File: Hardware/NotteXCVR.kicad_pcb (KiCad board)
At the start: 2 copper layers, 22 x 30 mm, 2 parts, among them J1 Bus_M.2_Socket_E, U1 XC7A50T-CPG236

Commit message: CSG325?
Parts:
- removed U1: XC7A50T-CPG236, Package_BGA:Xilinx_CPG236
- added R1: 100, Resistor_SMD:R_0402_1005Metric, F.Cu at (132.3, 104.9)
- added U2: XC7A35T-CSG325, Package_BGA:Xilinx_CSG325, F.Cu at (137.9, 125.0)

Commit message: PCIe
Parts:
- J1: value Bus_M.2_Socket_E -> Bus_PCI_Express_x1; footprint Connector_PCBEdge:M.2_2230-xx-E -> Connector_PCBEdge:BUS_PCIexpress_x1
- moved U2 65.9 mm to (89.9, 79.9), turned to 90 degrees
- moved R1 55.9 mm to (77.9, 92.0)
- moved J1 35.4 mm to (77.3, 102.7)
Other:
- board size 22 x 30 mm -> 20.3 x 8.4 mm

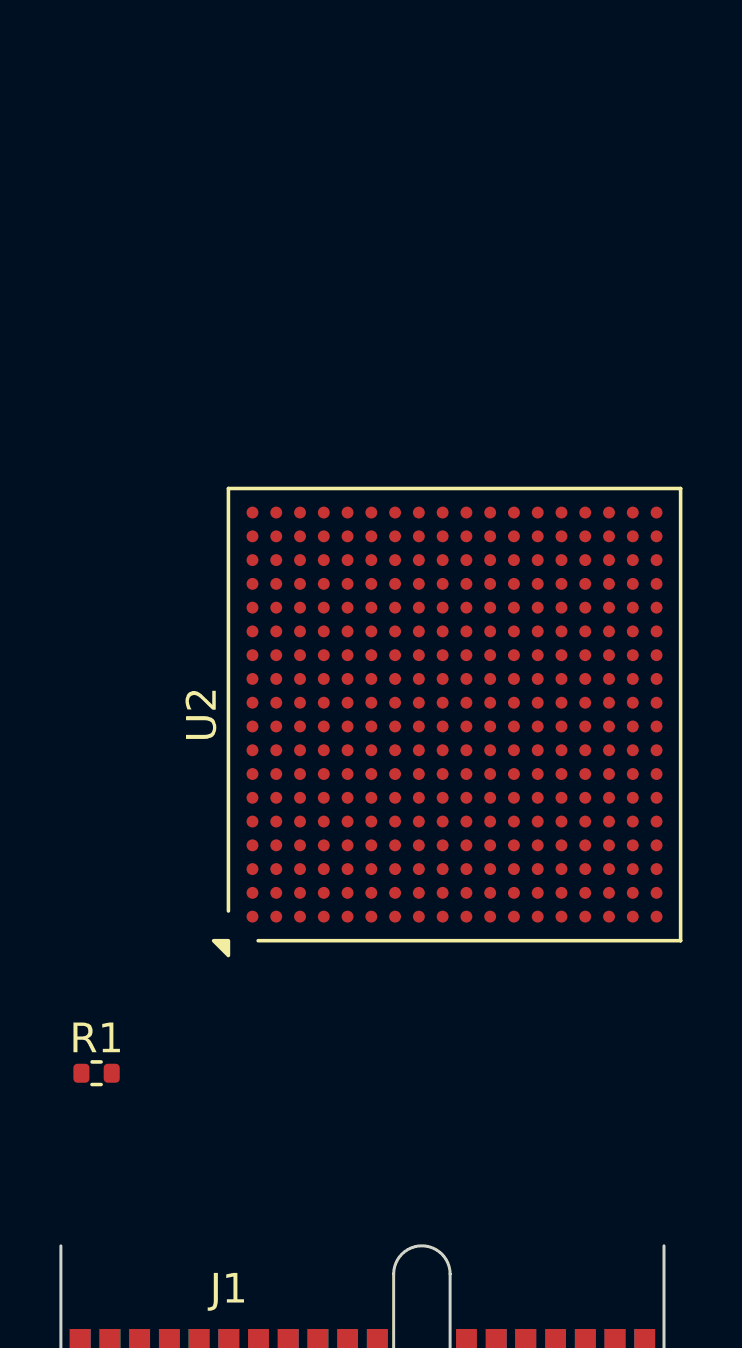
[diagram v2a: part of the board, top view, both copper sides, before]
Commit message: Added LGA connector, to be used for configuration interface
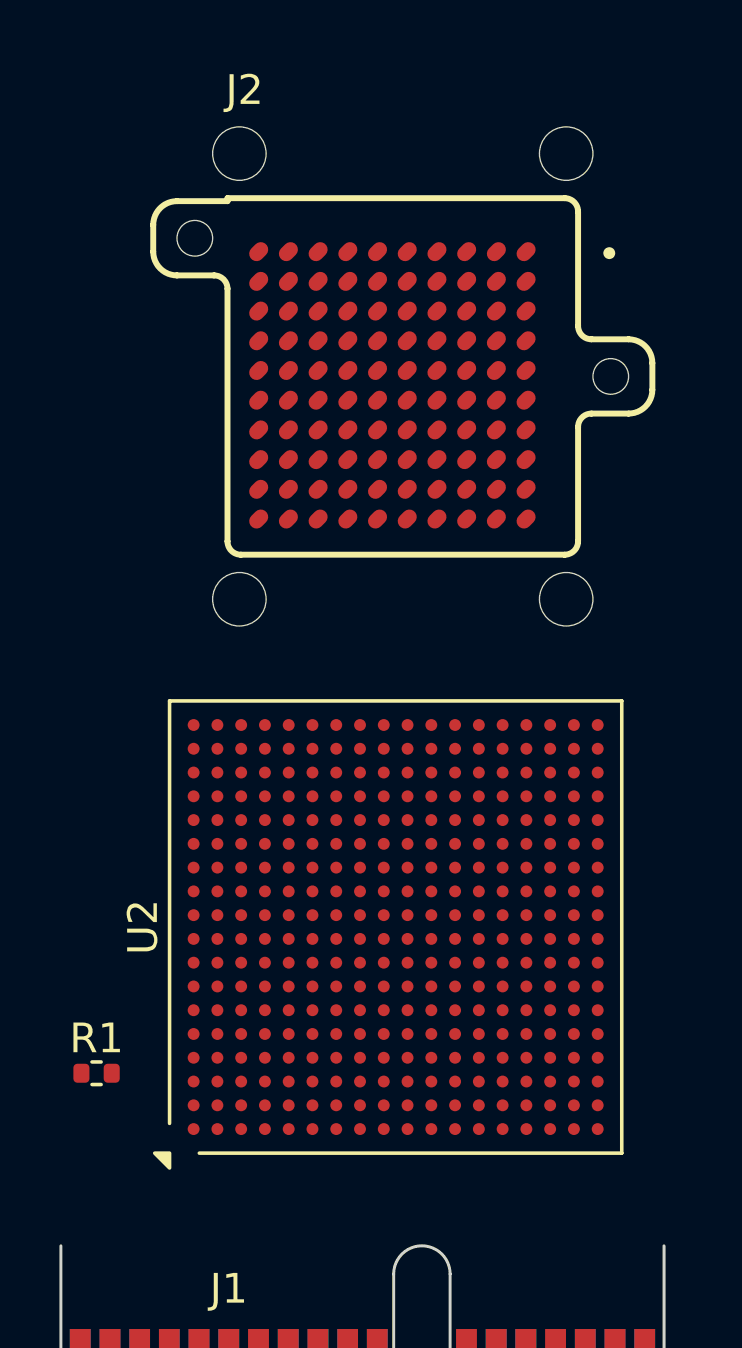
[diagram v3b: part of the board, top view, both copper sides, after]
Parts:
- added J2: GMI-10-2-1.27-G-10, GMI-10-2-1.27-G-10:SAMTEC_GMI-10-2-1.27-G-10, F.Cu at (88.2, 68.5)
- moved U2 7.42 mm to (88.0, 87.1)
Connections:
- R1 pad 1: unconnected-(R1-Pad1) -> Net-(R1-Pad1)
- R1 pad 2: unconnected-(R1-Pad2) -> Net-(U2D-MGTRREF_216)
- U2 pad A2: unconnected-(U2D-MGTAVTT-PadA2) -> Net-(R1-Pad1)
- U2 pad A6: unconnected-(U2D-MGTRREF_216-PadA6) -> Net-(U2D-MGTRREF_216)
- U2 pad C1: unconnected-(U2D-MGTAVTT-PadC1) -> Net-(R1-Pad1)
- U2 pad E1: unconnected-(U2D-MGTAVTT-PadE1) -> Net-(R1-Pad1)
- U2 pad F3: unconnected-(U2D-MGTAVTT-PadF3) -> Net-(R1-Pad1)
- U2 pad G2: unconnected-(U2D-MGTAVTT-PadG2) -> Net-(R1-Pad1)

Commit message: Trying to assign MGT lanes but I don't know how to do inter sheet connectivity yet
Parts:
- added C1: 0.01uF, Capacitor_SMD:C_0402_1005Metric, F.Cu at (91.3, 96.3)
- added C2: 0.01uF, Capacitor_SMD:C_0402_1005Metric, F.Cu at (92.4, 96.2)
- added C3: 0.22uF, Capacitor_SMD:C_0402_1005Metric, F.Cu at (94.3, 96.2)
- added C4: 0.22uF, Capacitor_SMD:C_0402_1005Metric, F.Cu at (95.5, 96.2)
- moved R1 2.11 mm to (77.9, 89.9)
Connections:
- net Net-(J1-+12V-PadA2) renamed +12V
- net Net-(J1-+3.3V-PadA10) renamed +3.3V
- net Net-(R1-Pad1) renamed MGTAVTT
- J1 pad A13: unconnected-(J1-REFCLK+-PadA13) -> Net-(J1-REFCLK+)
- J1 pad A14: unconnected-(J1-REFCLK--PadA14) -> Net-(J1-REFCLK-)
- J1 pad A16: unconnected-(J1-PERp0-PadA16) -> Net-(J1-PERp0)
- J1 pad A17: unconnected-(J1-PERn0-PadA17) -> Net-(J1-PERn0)
- J1 pad B14: unconnected-(J1-PETp0-PadB14) -> /PCIE_Edge/PCIE_TX_P
- J1 pad B15: unconnected-(J1-PETn0-PadB15) -> /PCIE_Edge/PCIE_TX_N
- U2 pad B4: unconnected-(U2D-MGTAVCC-PadB4) -> MGTAVCC
- U2 pad C3: unconnected-(U2C-MGTPRXN2_216-PadC3) -> /FPGA_MGT/MGT_LOOPBACK_N
- U2 pad C4: unconnected-(U2C-MGTPRXP2_216-PadC4) -> /FPGA_MGT/MGT_LOOPBACK_P
- U2 pad C5: unconnected-(U2D-MGTAVCC-PadC5) -> MGTAVCC
- U2 pad D1: unconnected-(U2C-MGTPTXN2_216-PadD1) -> /FPGA_MGT/MGT_LOOPBACK_N
- U2 pad D2: unconnected-(U2C-MGTPTXP2_216-PadD2) -> /FPGA_MGT/MGT_LOOPBACK_P
- U2 pad E5: unconnected-(U2D-MGTAVCC-PadE5) -> MGTAVCC
- U2 pad F5: unconnected-(U2D-MGTAVCC-PadF5) -> MGTAVCC
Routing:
- net Net-(U2D-MGTRREF_216): track 0.00 -> 2.76 mm

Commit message: Found the global labels
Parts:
- C1, C2, C3, C4: moved to B.Cu
- moved R1 9.49 mm to (87.1, 87.4)
- moved U2 9.49 mm to (97.1, 84.6)
- moved J2 3.68 mm to (86.7, 65.2)
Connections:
- C1 pad 1: /PCIE_Edge/PCIE_REFCLK_P -> PCIE_REFCLK_P
- C2 pad 1: /PCIE_Edge/PCIE_REFCLK_N -> PCIE_REFCLK_N
- C3 pad 2: /PCIE_Edge/PCIE_RX_P -> PCIE_RX_P
- C4 pad 2: /PCIE_Edge/PCIE_RX_N -> PCIE_RX_N
- J1 pad A12: Net-(J1-GND-PadA12) -> GND
- J1 pad A15: Net-(J1-GND-PadA12) -> GND
- J1 pad A18: Net-(J1-GND-PadA12) -> GND
- J1 pad A4: Net-(J1-GND-PadA12) -> GND
- J1 pad B13: Net-(J1-GND-PadA12) -> GND
- J1 pad B14: /PCIE_Edge/PCIE_TX_P -> PCIE_TX_P
- J1 pad B15: /PCIE_Edge/PCIE_TX_N -> PCIE_TX_N
- J1 pad B16: Net-(J1-GND-PadA12) -> GND
- J1 pad B18: Net-(J1-GND-PadA12) -> GND
- J1 pad B4: Net-(J1-GND-PadA12) -> GND
- J1 pad B7: Net-(J1-GND-PadA12) -> GND
- J2 pad A01: unconnected-(J2-PadA01) -> GND
- J2 pad A04: unconnected-(J2-PadA04) -> GND
- J2 pad A07: unconnected-(J2-PadA07) -> GND
- J2 pad A10: unconnected-(J2-PadA10) -> GND
- J2 pad D01: unconnected-(J2-PadD01) -> GND
- J2 pad D04: unconnected-(J2-PadD04) -> GND
- J2 pad D07: unconnected-(J2-PadD07) -> GND
- J2 pad D10: unconnected-(J2-PadD10) -> GND
- J2 pad G01: unconnected-(J2-PadG01) -> GND
- J2 pad G04: unconnected-(J2-PadG04) -> GND
- J2 pad G07: unconnected-(J2-PadG07) -> GND
- J2 pad G10: unconnected-(J2-PadG10) -> GND
- J2 pad J01: unconnected-(J2-PadJ01) -> GND
- J2 pad J04: unconnected-(J2-PadJ04) -> GND
- J2 pad J07: unconnected-(J2-PadJ07) -> GND
- J2 pad J10: unconnected-(J2-PadJ10) -> GND
- U2 pad A3: unconnected-(U2C-MGTPRXN1_216-PadA3) -> /FPGA_MGT/MGT_SMA_RX_N
- U2 pad A4: unconnected-(U2C-MGTPRXP1_216-PadA4) -> /FPGA_MGT/MGT_SMA_RX_P
- U2 pad B1: unconnected-(U2C-MGTPTXN3_216-PadB1) -> PCIE_TX_N
- U2 pad B2: unconnected-(U2C-MGTPTXP3_216-PadB2) -> PCIE_TX_P
- U2 pad B5: unconnected-(U2C-MGTREFCLK1N_216-PadB5) -> PCIE_REFCLK_N
- U2 pad B6: unconnected-(U2C-MGTREFCLK1P_216-PadB6) -> PCIE_REFCLK_P
- U2 pad D5: unconnected-(U2C-MGTREFCLK0N_216-PadD5) -> /FPGA_MGT/SMA_CLK_N
- U2 pad D6: unconnected-(U2C-MGTREFCLK0P_216-PadD6) -> /FPGA_MGT/SMA_CLK_P
- U2 pad F1: unconnected-(U2C-MGTPTXN1_216-PadF1) -> /FPGA_MGT/MGT_SMA_TX_N
- U2 pad F2: unconnected-(U2C-MGTPTXP1_216-PadF2) -> /FPGA_MGT/MGT_SMA_TX_P
- U2 pad G3: unconnected-(U2C-MGTPRXN3_216-PadG3) -> PCIE_RX_N
- U2 pad G4: unconnected-(U2C-MGTPRXP3_216-PadG4) -> PCIE_RX_P
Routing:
- net /FPGA_MGT/MGT_LOOPBACK_P: track 0.00 -> 2.61 mm
- net /FPGA_MGT/MGT_LOOPBACK_N: track 0.00 -> 2.58 mm
- net PCIE_RX_P: track 0.00 -> 0.43 mm, vias 0 -> 1
- net PCIE_RX_N: track 0.00 -> 0.41 mm, vias 0 -> 1

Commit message: Is this orientation better
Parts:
- added J3: Conn_Coaxial, Connector_Coaxial:U.FL_Hirose_U.FL-R-SMT-1_Vertical, F.Cu at (85.1, 74.1)
- added J4: Conn_Coaxial, Connector_Coaxial:U.FL_Hirose_U.FL-R-SMT-1_Vertical, F.Cu at (87.1, 69.7)
- added J5: Conn_Coaxial, Connector_Coaxial:U.FL_Hirose_U.FL-R-SMT-1_Vertical, F.Cu at (91.2, 74.1)
- added J6: Conn_Coaxial, Connector_Coaxial:U.FL_Hirose_U.FL-R-SMT-1_Vertical, F.Cu at (93.2, 69.8)
- added J7: Conn_Coaxial, Connector_Coaxial:U.FL_Hirose_U.FL-R-SMT-1_Vertical, F.Cu at (79.2, 74.1)
- added J8: Conn_Coaxial, Connector_Coaxial:U.FL_Hirose_U.FL-R-SMT-1_Vertical, F.Cu at (81.3, 69.6)
- moved U2 10.0 mm to (87.1, 84.9), turned to 180 degrees
- moved R1 7.30 mm to (90.5, 93.9), turned to 180 degrees
- moved J2 6.25 mm to (86.8, 58.9)
- moved C2 0.11 mm to (92.4, 96.3)
- moved C1 0.11 mm to (91.4, 96.4)
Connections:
- C3 pad 2: PCIE_RX_P -> PCIE_TX_P
- C4 pad 2: PCIE_RX_N -> PCIE_TX_N
- J1 pad B14: PCIE_TX_P -> PCIE_RX_P
- J1 pad B15: PCIE_TX_N -> PCIE_RX_N
- U2 pad A1: unconnected-(U2F-GND-PadA1) -> GND
- U2 pad A11: unconnected-(U2F-GND-PadA11) -> GND
- U2 pad A16: unconnected-(U2A-VCCO_15-PadA16) -> Net-(U2A-VCCO_15-PadA16)
- U2 pad A18: unconnected-(U2F-GND-PadA18) -> GND
- U2 pad A3: /FPGA_MGT/MGT_SMA_RX_N -> /FPGA_MGT/MGT_UFL_RX_N
- U2 pad A4: /FPGA_MGT/MGT_SMA_RX_P -> /FPGA_MGT/MGT_UFL_RX_P
- U2 pad A5: unconnected-(U2F-GND-PadA5) -> GND
- U2 pad A7: unconnected-(U2F-GND-PadA7) -> GND
- U2 pad A8: unconnected-(U2F-GND-PadA8) -> GND
- U2 pad B13: unconnected-(U2A-VCCO_15-PadB13) -> Net-(U2A-VCCO_15-PadA16)
- U2 pad B18: unconnected-(U2F-GND-PadB18) -> GND
- U2 pad B3: unconnected-(U2F-GND-PadB3) -> GND
- U2 pad B7: unconnected-(U2F-GND-PadB7) -> GND
- U2 pad B8: unconnected-(U2F-GND-PadB8) -> GND
- U2 pad C10: unconnected-(U2A-VCCO_15-PadC10) -> Net-(U2A-VCCO_15-PadA16)
- U2 pad C15: unconnected-(U2F-GND-PadC15) -> GND
- U2 pad C2: unconnected-(U2F-GND-PadC2) -> GND
- U2 pad C6: unconnected-(U2F-GND-PadC6) -> GND
- U2 pad C7: unconnected-(U2F-GND-PadC7) -> GND
- U2 pad D12: unconnected-(U2F-GND-PadD12) -> GND
- U2 pad D17: unconnected-(U2A-VCCO_15-PadD17) -> Net-(U2A-VCCO_15-PadA16)
- U2 pad D3: unconnected-(U2F-GND-PadD3) -> GND
- U2 pad D4: unconnected-(U2F-GND-PadD4) -> GND
- U2 pad D5: /FPGA_MGT/SMA_CLK_N -> /FPGA_MGT/UFL_CLK_N
- U2 pad D6: /FPGA_MGT/SMA_CLK_P -> /FPGA_MGT/UFL_CLK_P
- U2 pad D7: unconnected-(U2F-GND-PadD7) -> GND
- U2 pad E11: unconnected-(U2F-VCCBATT_0-PadE11) -> +1V8
- U2 pad E14: unconnected-(U2A-VCCO_15-PadE14) -> Net-(U2A-VCCO_15-PadA16)
- U2 pad E2: unconnected-(U2F-GND-PadE2) -> GND
- U2 pad E6: unconnected-(U2F-GND-PadE6) -> GND
- U2 pad E7: unconnected-(U2F-GND-PadE7) -> GND
- U2 pad E9: unconnected-(U2F-GND-PadE9) -> GND
- U2 pad F1: /FPGA_MGT/MGT_SMA_TX_N -> /FPGA_MGT/MGT_UFL_TX_N
- U2 pad F10: unconnected-(U2F-GND-PadF10) -> GND
- U2 pad F11: unconnected-(U2F-VCCBRAM-PadF11) -> +1V0
- U2 pad F16: unconnected-(U2F-GND-PadF16) -> GND
- U2 pad F2: /FPGA_MGT/MGT_SMA_TX_P -> /FPGA_MGT/MGT_UFL_TX_P
- U2 pad F4: unconnected-(U2F-GND-PadF4) -> GND
- U2 pad F6: unconnected-(U2F-GND-PadF6) -> GND
- U2 pad F7: unconnected-(U2F-VCCINT-PadF7) -> +1V0
- U2 pad F9: unconnected-(U2F-VCCINT-PadF9) -> +1V0
- U2 pad G1: unconnected-(U2F-GND-PadG1) -> GND
- U2 pad G10: unconnected-(U2F-VCCBRAM-PadG10) -> +1V0
- U2 pad G11: unconnected-(U2F-GND-PadG11) -> GND
- U2 pad G12: unconnected-(U2F-VCCAUX-PadG12) -> +1V8
- U2 pad G13: unconnected-(U2F-GND-PadG13) -> GND
- U2 pad G18: unconnected-(U2A-VCCO_15-PadG18) -> Net-(U2A-VCCO_15-PadA16)
- U2 pad G5: unconnected-(U2F-GND-PadG5) -> GND
- U2 pad G6: unconnected-(U2F-GND-PadG6) -> GND
- U2 pad G7: unconnected-(U2F-GND-PadG7) -> GND
- U2 pad G8: unconnected-(U2F-VCCINT-PadG8) -> +1V0
- U2 pad G9: unconnected-(U2F-GND-PadG9) -> GND
- U2 pad H10: unconnected-(U2F-GND-PadH10) -> GND
- U2 pad H11: unconnected-(U2F-VCCBRAM-PadH11) -> +1V0
- U2 pad H12: unconnected-(U2F-GND-PadH12) -> GND
- U2 pad H13: unconnected-(U2F-VCCAUX-PadH13) -> +1V8
- U2 pad H15: unconnected-(U2A-VCCO_15-PadH15) -> Net-(U2A-VCCO_15-PadA16)
- U2 pad H3: unconnected-(U2F-GND-PadH3) -> GND
- U2 pad H4: unconnected-(U2F-GND-PadH4) -> GND
- U2 pad H5: unconnected-(U2F-GND-PadH5) -> GND
- U2 pad H6: unconnected-(U2F-GND-PadH6) -> GND
- U2 pad H7: unconnected-(U2F-VCCINT-PadH7) -> +1V0
- U2 pad H8: unconnected-(U2F-GND-PadH8) -> GND
- U2 pad H9: unconnected-(U2F-VCCINT-PadH9) -> +1V0
- U2 pad J1: unconnected-(U2F-GND-PadJ1) -> GND
- U2 pad J10: unconnected-(U2F-VCCADC_0-PadJ10) -> +1V8
- U2 pad J11: unconnected-(U2F-GND-PadJ11) -> GND
- U2 pad J12: unconnected-(U2F-VCCINT-PadJ12) -> +1V0
- U2 pad J13: unconnected-(U2F-GND-PadJ13) -> GND
- U2 pad J17: unconnected-(U2F-GND-PadJ17) -> GND
- U2 pad J2: unconnected-(U2F-GND-PadJ2) -> GND
- U2 pad J3: unconnected-(U2F-GND-PadJ3) -> GND
- U2 pad J7: unconnected-(U2F-GND-PadJ7) -> GND
- U2 pad J8: unconnected-(U2F-VCCINT-PadJ8) -> +1V0
- U2 pad J9: unconnected-(U2F-GNDADC_0-PadJ9) -> GND
- U2 pad K11: unconnected-(U2F-VCCINT-PadK11) -> +1V0
- U2 pad K12: unconnected-(U2F-GND-PadK12) -> GND
- U2 pad K13: unconnected-(U2F-VCCAUX-PadK13) -> +1V8
- U2 pad K14: unconnected-(U2F-GND-PadK14) -> GND
- U2 pad K4: unconnected-(U2F-GND-PadK4) -> GND
- U2 pad K7: unconnected-(U2F-VCCINT-PadK7) -> +1V0
- U2 pad K8: unconnected-(U2F-GND-PadK8) -> GND
- U2 pad L1: unconnected-(U2F-GND-PadL1) -> GND
- U2 pad L11: unconnected-(U2F-GND-PadL11) -> GND
- U2 pad L12: unconnected-(U2F-VCCINT-PadL12) -> +1V0
- U2 pad L13: unconnected-(U2F-GND-PadL13) -> GND
- U2 pad L16: unconnected-(U2A-VCCO_14-PadL16) -> Net-(U2A-VCCO_14-PadL16)
- U2 pad L6: unconnected-(U2B-VCCO_34-PadL6) -> Net-(U2B-VCCO_34-PadL6)
- U2 pad L7: unconnected-(U2F-GND-PadL7) -> GND
- U2 pad L8: unconnected-(U2F-VCCINT-PadL8) -> +1V0
- U2 pad M11: unconnected-(U2F-VCCINT-PadM11) -> +1V0
- U2 pad M12: unconnected-(U2F-GND-PadM12) -> GND
- U2 pad M13: unconnected-(U2F-VCCAUX-PadM13) -> +1V8
- U2 pad M18: unconnected-(U2F-GND-PadM18) -> GND
- U2 pad M3: unconnected-(U2B-VCCO_34-PadM3) -> Net-(U2B-VCCO_34-PadL6)
- U2 pad M7: unconnected-(U2F-VCCINT-PadM7) -> +1V0
- U2 pad M8: unconnected-(U2F-GND-PadM8) -> GND
- U2 pad N10: unconnected-(U2F-VCCINT-PadN10) -> +1V0
- U2 pad N11: unconnected-(U2F-GND-PadN11) -> GND
- U2 pad N12: unconnected-(U2F-VCCINT-PadN12) -> +1V0
- U2 pad N13: unconnected-(U2F-GND-PadN13) -> GND
- U2 pad N15: unconnected-(U2F-GND-PadN15) -> GND
- U2 pad N5: unconnected-(U2F-GND-PadN5) -> GND
- U2 pad N7: unconnected-(U2F-GND-PadN7) -> GND
- U2 pad N8: unconnected-(U2F-VCCINT-PadN8) -> +1V0
- U2 pad N9: unconnected-(U2F-GND-PadN9) -> GND
- U2 pad P11: unconnected-(U2F-VCCINT-PadP11) -> +1V0
- U2 pad P12: unconnected-(U2F-GND-PadP12) -> GND
- U2 pad P13: unconnected-(U2F-VCCAUX-PadP13) -> +1V8
- U2 pad P17: unconnected-(U2A-VCCO_14-PadP17) -> Net-(U2A-VCCO_14-PadL16)
- U2 pad P2: unconnected-(U2F-GND-PadP2) -> GND
- U2 pad P7: unconnected-(U2B-VCCO_34-PadP7) -> Net-(U2B-VCCO_34-PadL6)
- U2 pad P8: unconnected-(U2F-GND-PadP8) -> GND
- U2 pad P9: unconnected-(U2F-VCCINT-PadP9) -> +1V0
- U2 pad R14: unconnected-(U2A-VCCO_14-PadR14) -> Net-(U2A-VCCO_14-PadL16)
- U2 pad R4: unconnected-(U2B-VCCO_34-PadR4) -> Net-(U2B-VCCO_34-PadL6)
- U2 pad R9: unconnected-(U2F-GND-PadR9) -> GND
- U2 pad T1: unconnected-(U2B-VCCO_34-PadT1) -> Net-(U2B-VCCO_34-PadL6)
- U2 pad T11: unconnected-(U2A-VCCO_14-PadT11) -> Net-(U2A-VCCO_14-PadL16)
- U2 pad T16: unconnected-(U2F-GND-PadT16) -> GND
- U2 pad T6: unconnected-(U2F-GND-PadT6) -> GND
- U2 pad U13: unconnected-(U2F-GND-PadU13) -> GND
- U2 pad U18: unconnected-(U2A-VCCO_14-PadU18) -> Net-(U2A-VCCO_14-PadL16)
- U2 pad U3: unconnected-(U2F-GND-PadU3) -> GND
- U2 pad U8: unconnected-(U2A-VCCO_14-PadU8) -> Net-(U2A-VCCO_14-PadL16)
- U2 pad V1: unconnected-(U2F-GND-PadV1) -> GND
- U2 pad V10: unconnected-(U2F-GND-PadV10) -> GND
- U2 pad V15: unconnected-(U2A-VCCO_14-PadV15) -> Net-(U2A-VCCO_14-PadL16)
- U2 pad V18: unconnected-(U2F-GND-PadV18) -> GND
- U2 pad V5: unconnected-(U2B-VCCO_34-PadV5) -> Net-(U2B-VCCO_34-PadL6)
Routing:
- net Net-(U2D-MGTRREF_216): track 2.76 -> 2.22 mm
- net PCIE_RX_P: track 0.43 -> 0.00 mm, vias 1 -> 0
- net PCIE_RX_N: track 0.41 -> 0.00 mm, vias 1 -> 0
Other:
- board size 20.3 x 8.4 mm -> 20.3 x 48.8 mm

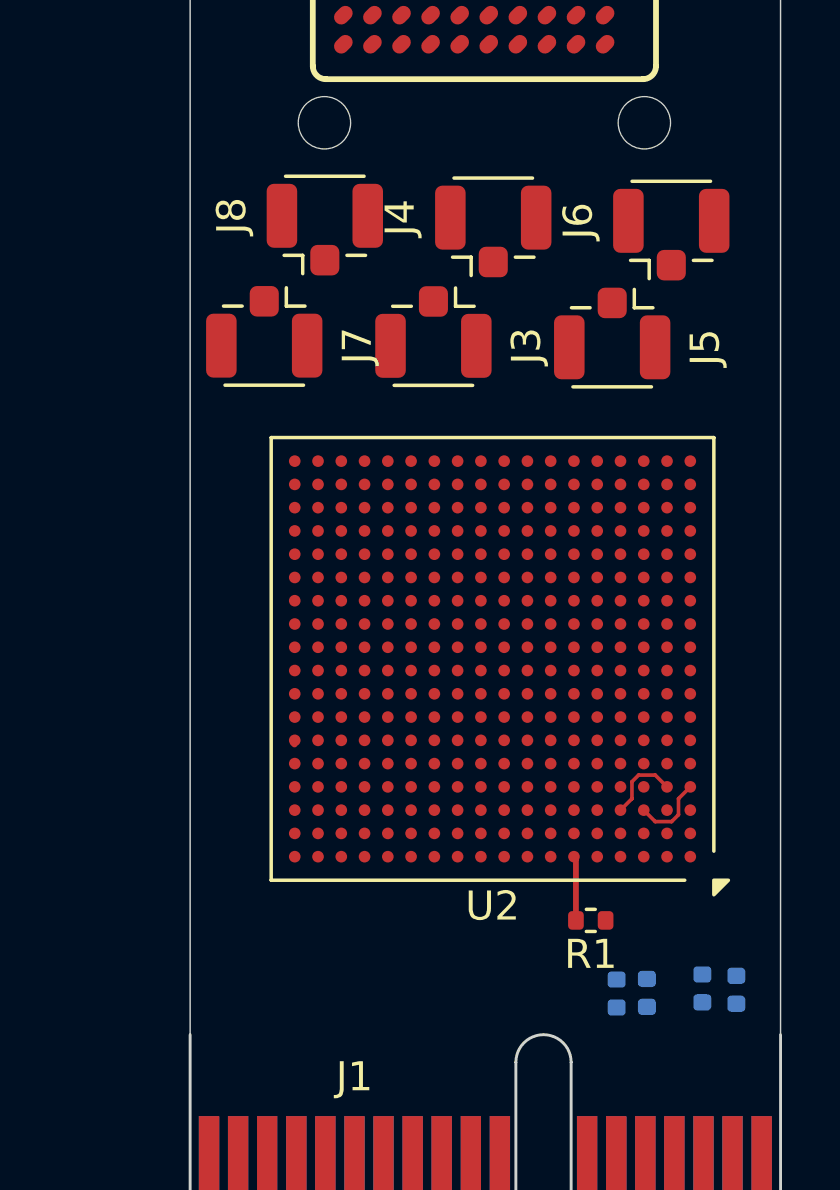
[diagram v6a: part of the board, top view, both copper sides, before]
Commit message: This might be better orientation/pin choices
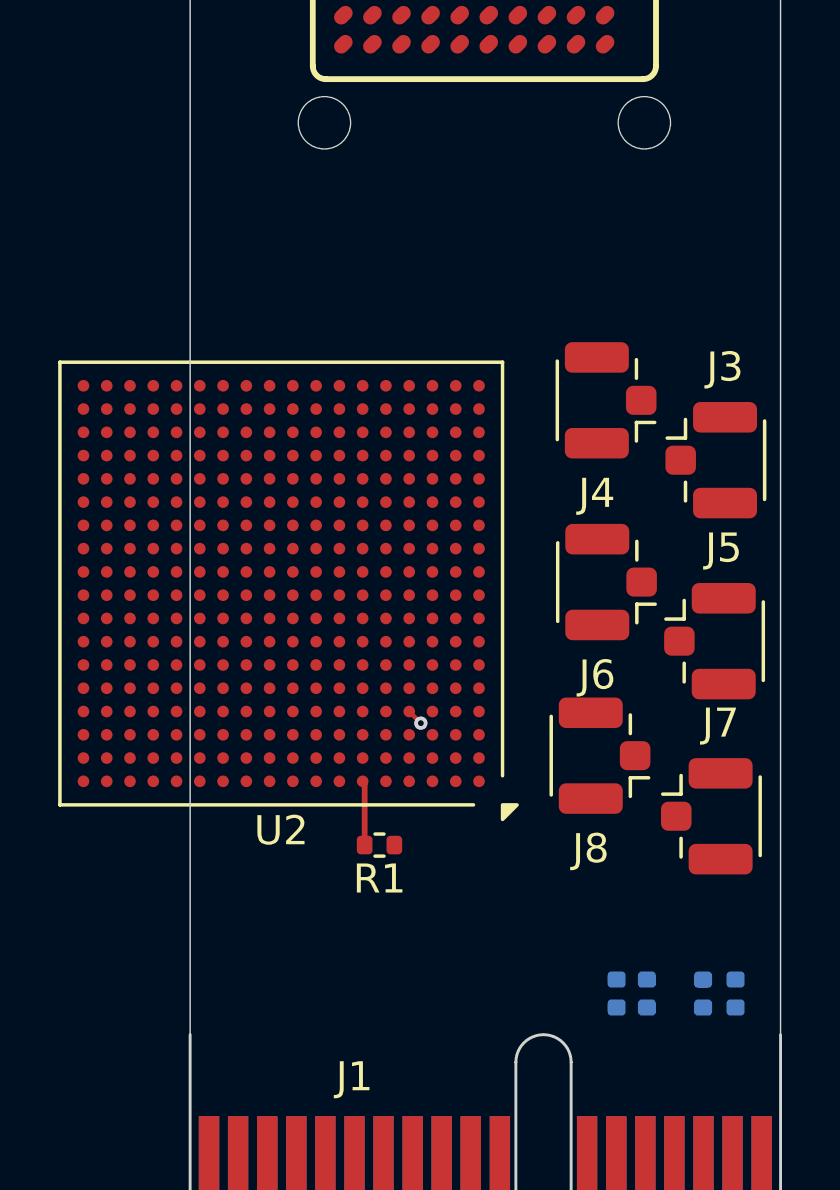
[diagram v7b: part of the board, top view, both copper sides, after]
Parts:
- moved J7 22.5 mm to (94.9, 90.3), turned to 0 degrees
- moved J8 20.7 mm to (90.5, 88.2), turned to 180 degrees
- moved J6 12.7 mm to (90.7, 82.2), turned to 180 degrees
- moved J5 10.8 mm to (95.0, 84.3), turned to 0 degrees
- moved J3 10.8 mm to (95.1, 78.0), turned to 0 degrees
- moved U2 7.71 mm to (79.8, 82.3)
- moved R1 7.71 mm to (83.2, 91.3)
- moved J4 7.22 mm to (90.7, 76.0), turned to 180 degrees
- moved C3 0.18 mm to (94.3, 96.4)
- moved C4 0.13 mm to (95.5, 96.4)
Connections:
- U2 pad A3: /FPGA_MGT/MGT_UFL_RX_N -> unconnected-(U2C-MGTPRXN1_216-PadA3)
- U2 pad A4: /FPGA_MGT/MGT_UFL_RX_P -> unconnected-(U2C-MGTPRXP1_216-PadA4)
- U2 pad B1: PCIE_TX_N -> unconnected-(U2C-MGTPTXN3_216-PadB1)
- U2 pad B2: PCIE_TX_P -> unconnected-(U2C-MGTPTXP3_216-PadB2)
- U2 pad B5: PCIE_REFCLK_N -> /FPGA_MGT/UFL_CLK_N
- U2 pad B6: PCIE_REFCLK_P -> /FPGA_MGT/UFL_CLK_P
- U2 pad C3: /FPGA_MGT/MGT_LOOPBACK_N -> PCIE_RX_N
- U2 pad C4: /FPGA_MGT/MGT_LOOPBACK_P -> PCIE_RX_P
- U2 pad D1: /FPGA_MGT/MGT_LOOPBACK_N -> PCIE_TX_N
- U2 pad D2: /FPGA_MGT/MGT_LOOPBACK_P -> PCIE_TX_P
- U2 pad D5: /FPGA_MGT/UFL_CLK_N -> PCIE_REFCLK_N
- U2 pad D6: /FPGA_MGT/UFL_CLK_P -> PCIE_REFCLK_P
- U2 pad E3: unconnected-(U2C-MGTPRXN0_216-PadE3) -> /FPGA_MGT/MGT_UFL_RX_N
- U2 pad E4: unconnected-(U2C-MGTPRXP0_216-PadE4) -> /FPGA_MGT/MGT_UFL_RX_P
- U2 pad F1: /FPGA_MGT/MGT_UFL_TX_N -> unconnected-(U2C-MGTPTXN1_216-PadF1)
- U2 pad F2: /FPGA_MGT/MGT_UFL_TX_P -> unconnected-(U2C-MGTPTXP1_216-PadF2)
- U2 pad G3: PCIE_RX_N -> unconnected-(U2C-MGTPRXN3_216-PadG3)
- U2 pad G4: PCIE_RX_P -> unconnected-(U2C-MGTPRXP3_216-PadG4)
- U2 pad H1: unconnected-(U2C-MGTPTXN0_216-PadH1) -> /FPGA_MGT/MGT_UFL_TX_N
- U2 pad H2: unconnected-(U2C-MGTPTXP0_216-PadH2) -> /FPGA_MGT/MGT_UFL_TX_P
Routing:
- net /FPGA_MGT/MGT_LOOPBACK_P: track 2.61 -> 0.00 mm
- net /FPGA_MGT/MGT_LOOPBACK_N: track 2.58 -> 0.00 mm
- net GND: track 0.00 -> 0.57 mm, vias 0 -> 1
